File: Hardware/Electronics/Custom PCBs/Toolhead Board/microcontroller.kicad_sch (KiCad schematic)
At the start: 35 parts, among them J1 USB C Receptacle, J2 Conn_02x08_Odd_Even, J3 Conn_02x08_Odd_Even, J4 Conn_02x08_Odd_Even, J5 Conn_02x04_Odd_Even, J6 Conn_02x04_Odd_Even, SW1 BOOT, SW2 RESET, U3 RP2040, U4 W25Q128JVS, Y1 12MHz/12pF/50Ω/20ppm

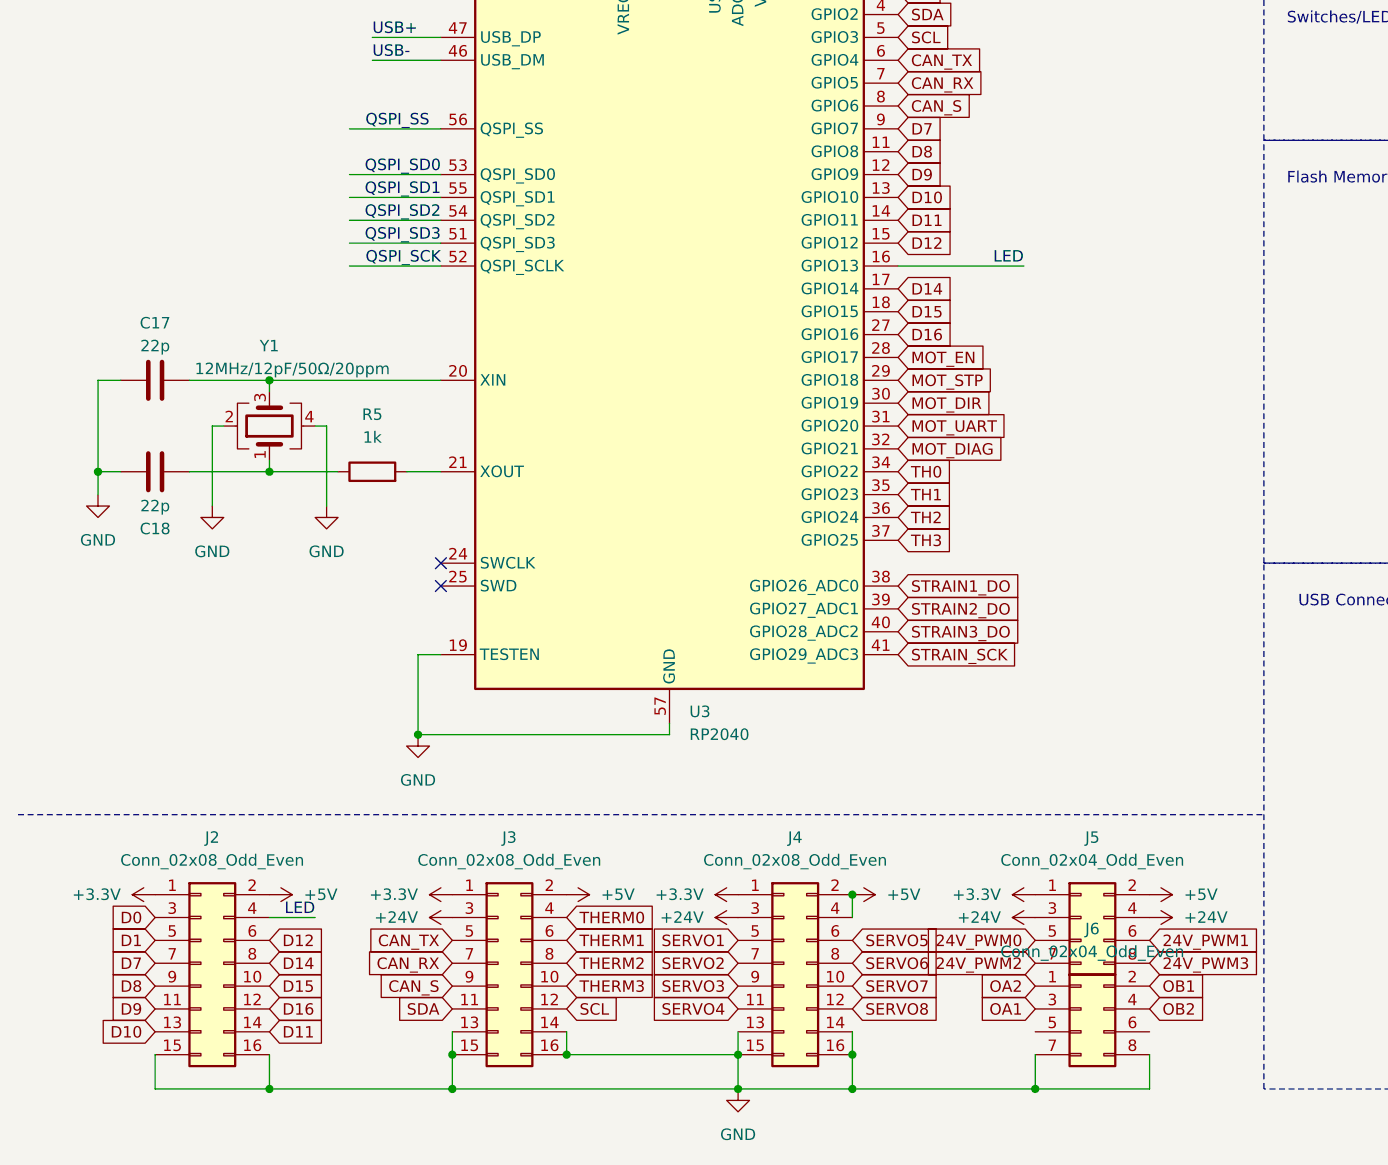
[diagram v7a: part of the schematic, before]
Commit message: Update toolhead layout
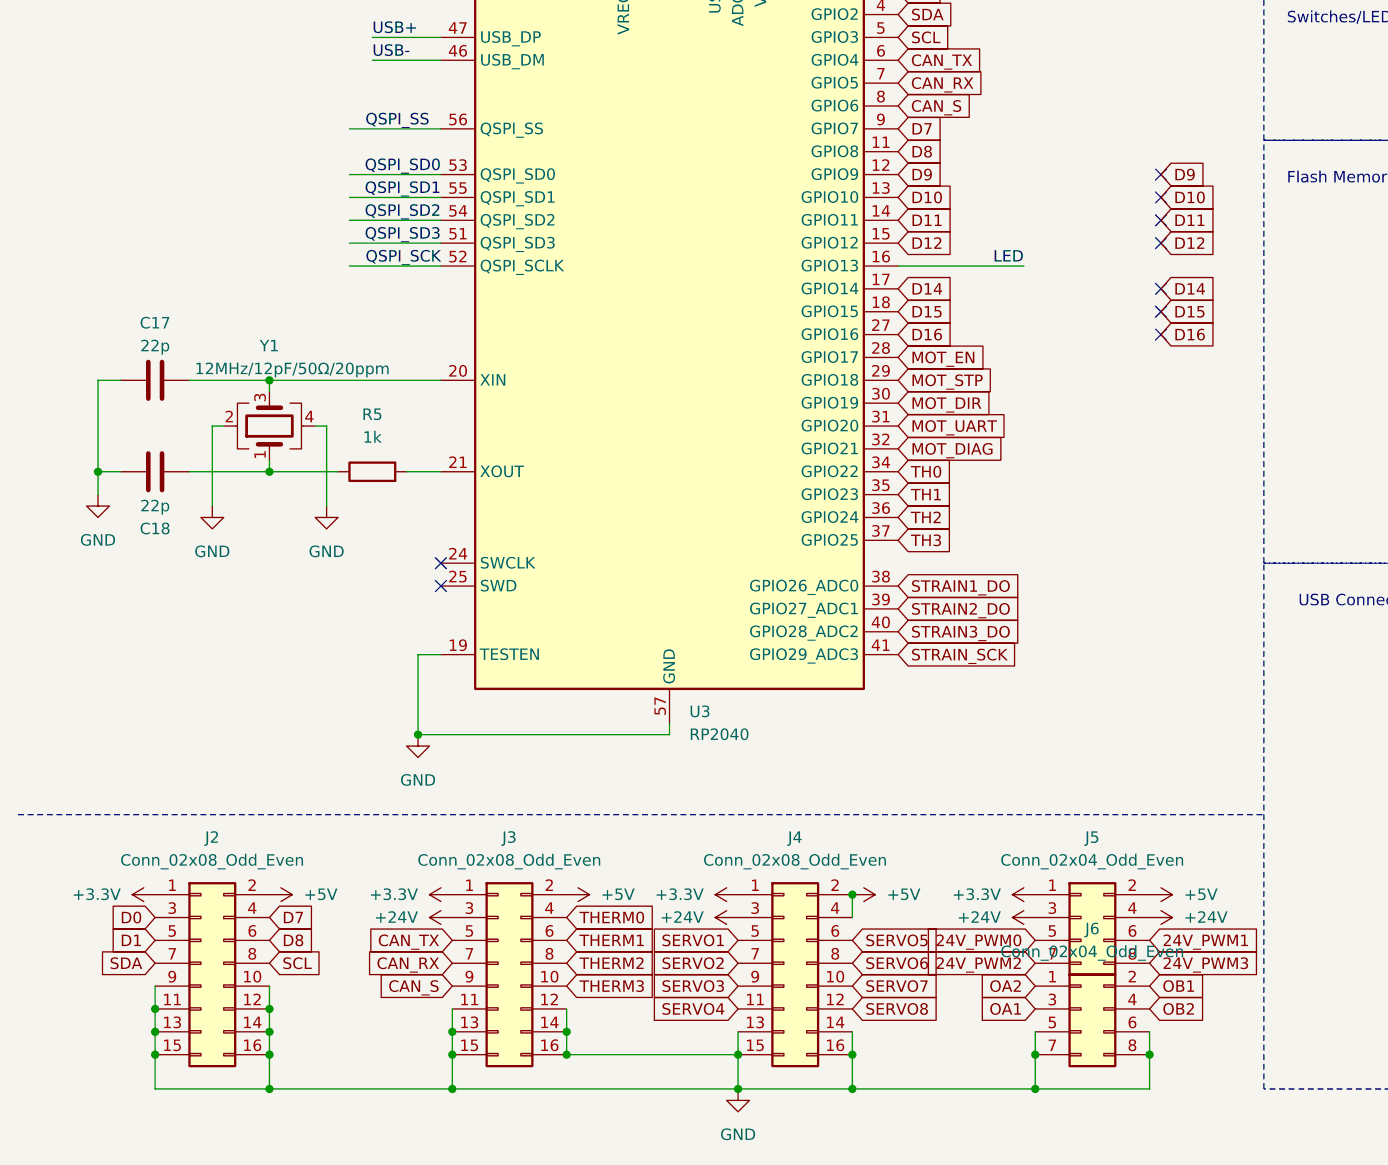
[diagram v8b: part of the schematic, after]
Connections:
- net D10: no longer J2.13 (Pin_13)
- net D11: no longer J2.14 (Pin_14)
- net D12: no longer J2.6 (Pin_6)
- net D14: no longer J2.8 (Pin_8)
- net D15: no longer J2.10 (Pin_10)
- net D16: no longer J2.12 (Pin_12)
- net D7: now also J2.4 (Pin_4); no longer J2.7 (Pin_7)
- net D8: now also J2.6 (Pin_6); no longer J2.9 (Pin_9)
- net D9: no longer J2.11 (Pin_11)
- net GND: now also J2.10 (Pin_10), J2.11 (Pin_11), J2.12 (Pin_12), J2.13 (Pin_13), J2.14 (Pin_14), J2.9 (Pin_9), J3.11 (Pin_11), J3.12 (Pin_12), J6.5 (Pin_5), J6.6 (Pin_6)
- net LED: no longer J2.4 (Pin_4)
- net SCL: now also J2.8 (Pin_8); no longer J3.12 (Pin_12)
- net SDA: now also J2.7 (Pin_7); no longer J3.11 (Pin_11)
- no-connect marks 4 -> 11
